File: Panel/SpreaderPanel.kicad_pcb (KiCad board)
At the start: 2 copper layers, 50 x 200 mm, 7 parts

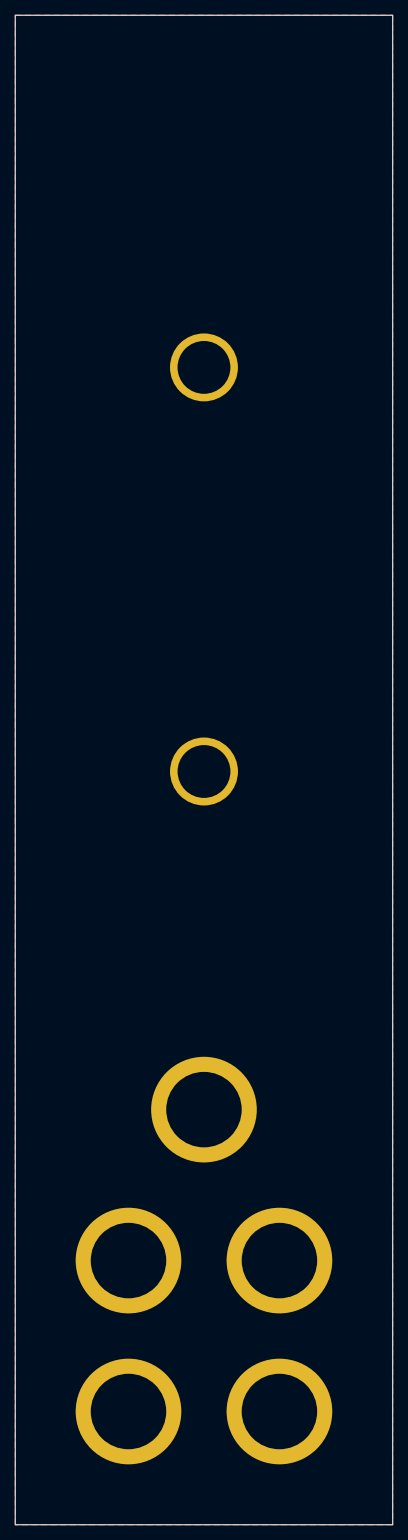
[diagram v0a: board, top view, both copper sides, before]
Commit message: Add panel text
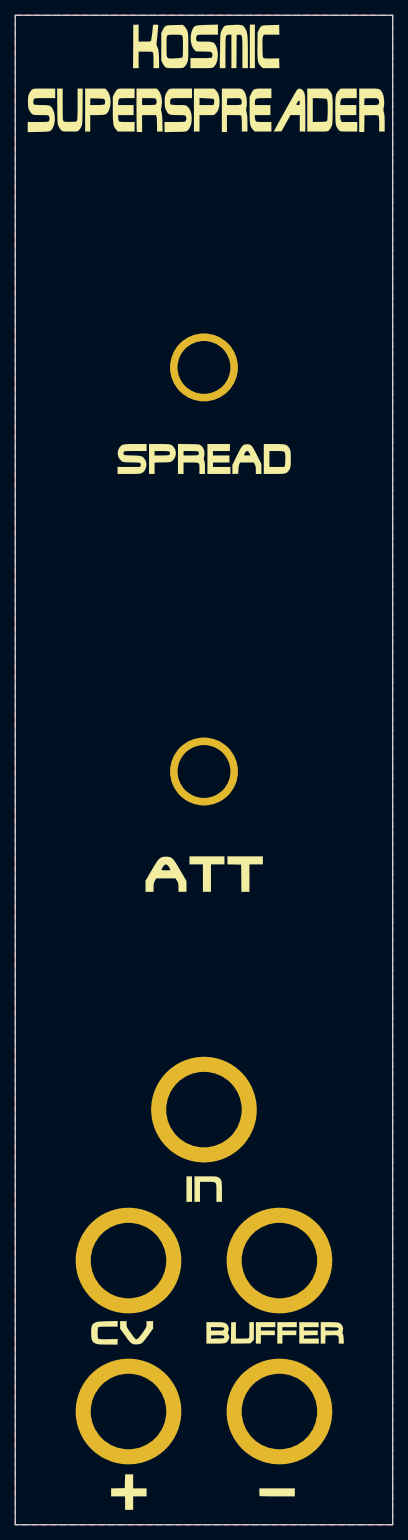
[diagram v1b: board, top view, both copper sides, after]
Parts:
- added G***: LOGO, Sonosus:SuperSilk, F.Cu at (126.9, 125.8)
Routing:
- added copper zone on B.Cu, net GND

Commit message: Add JLC order no and licensing info
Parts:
- added REF**: Kosmo_Panel_Slotted_Mounting_Hole, Sonosus:Kosmo_Panel_Slotted_Mounting_Hole, F.Cu at (104.9, 222.8)
- added REF**: Kosmo_Panel_Slotted_Mounting_Hole, Sonosus:Kosmo_Panel_Slotted_Mounting_Hole, F.Cu at (145.9, 222.8)
- added REF**: Kosmo_Panel_Slotted_Mounting_Hole, Sonosus:Kosmo_Panel_Slotted_Mounting_Hole, F.Cu at (145.9, 28.8)
- added REF**: Kosmo_Panel_Slotted_Mounting_Hole, Sonosus:Kosmo_Panel_Slotted_Mounting_Hole, F.Cu at (104.9, 28.8)
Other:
- board text added: "JLCJLCJLCJLC"
- board text added: "SS-06 Kosmic Superspreader CC-BY-SA Panel by Sonosus June 2021"
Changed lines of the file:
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@@
   (general
     (thickness 1.6)
-    (drawings 4)
+    (drawings 6)
     (tracks 0)
     (zones 0)
-    (modules 8)
+    (modules 12)
     (nets 2)
   )
@@
     (mod_text_size 1 1)
     (mod_text_width 0.15)
-    (pad_size 14 14)
-    (pad_drill 10)
+    (pad_size 6.8 4)
+    (pad_drill 6)
     (pad_to_mask_clearance 0)
     (aux_axis_origin 0 0)
@@
     (uvia_drill 0.1)
     (add_net GND)
+  )
+  (module Sonosus:Kosmo_Panel_Slotted_Mounting_Hole (layer F.Cu)
+    (at 104.873 222.81)
+    (descr "Mounting Hole 3.2mm, M3")
+    (tags "mounting hole 3.2mm m3")
+    (attr virtual)
+    (fp_text reference REF** (at 1.4 -4.2) (layer F.SilkS) hide
+      (effects (font (size 1 1) (thickness 0.15)))
+    )
+    (fp_text value Kosmo_Panel_Slotted_Mounting_Hole (at 1.4 4.2) (layer F.Fab)
+      (effects (font (size 1 1) (thickness 0.15)))
+    )
+    (fp_line (start 0 3.25) (end 2.8 3.25) (layer F.CrtYd) (width 0.05))
+    (fp_line (start 0 -3.25) (end 2.8 -3.25) (layer F.CrtYd) (width 0.05))
+    (fp_line (start 0 3) (end 2.8 3) (layer Cmts.User) (width 0.12))
+    (fp_line (start 0 -3) (end 2.8 -3) (layer Cmts.User) (width 0.12))
+    (fp_text user %R (at 1.7 0) (layer F.Fab)
+      (effects (font (size 1 1) (thickness 0.15)))
+    )
+    (fp_arc (start 2.8 0) (end 2.8 3) (angle -180) (layer Cmts.User) (width 0.12))
+    (fp_arc (start 0 0) (end 0 -3) (angle -180) (layer Cmts.User) (width 0.12))
+    (fp_arc (start 2.8 0) (end 2.8 3.25) (angle -180) (layer F.CrtYd) (width 0.05))
+    (fp_arc (start 0 0) (end 0 3.25) (angle 180) (layer F.CrtYd) (width 0.05))
+    (pad 1 thru_hole oval (at 1.4 0) (size 6.8 4) (drill oval 6 3.2) (layers *.Cu *.Mask)
+      (net 1 GND))
+  )
+  (module Sonosus:Kosmo_Panel_Slotted_Mounting_Hole (layer F.Cu)
+    (at 145.873 222.81)
+    (descr "Mounting Hole 3.2mm, M3")
+    (tags "mounting hole 3.2mm m3")
+    (attr virtual)
+    (fp_text reference REF** (at 1.4 -4.2) (layer F.SilkS) hide
+      (effects (font (size 1 1) (thickness 0.15)))
+    )
+    (fp_text value Kosmo_Panel_Slotted_Mounting_Hole (at 1.4 4.2) (layer F.Fab)
+      (effects (font (size 1 1) (thickness 0.15)))
+    )
+    (fp_line (start 0 3.25) (end 2.8 3.25) (layer F.CrtYd) (width 0.05))
+    (fp_line (start 0 -3.25) (end 2.8 -3.25) (layer F.CrtYd) (width 0.05))
+    (fp_line (start 0 3) (end 2.8 3) (layer Cmts.User) (width 0.12))
+    (fp_line (start 0 -3) (end 2.8 -3) (layer Cmts.User) (width 0.12))
+    (fp_text user %R (at 1.7 0) (layer F.Fab)
+      (effects (font (size 1 1) (thickness 0.15)))
+    )
+    (fp_arc (start 2.8 0) (end 2.8 3) (angle -180) (layer Cmts.User) (width 0.12))
+    (fp_arc (start 0 0) (end 0 -3) (angle -180) (layer Cmts.User) (width 0.12))
+    (fp_arc (start 2.8 0) (end 2.8 3.25) (angle -180) (layer F.CrtYd) (width 0.05))
+    (fp_arc (start 0 0) (end 0 3.25) (angle 180) (layer F.CrtYd) (width 0.05))
+    (pad 1 thru_hole oval (at 1.4 0) (size 6.8 4) (drill oval 6 3.2) (layers *.Cu *.Mask)
+      (net 1 GND))
+  )
+  (module Sonosus:Kosmo_Panel_Slotted_Mounting_Hole (layer F.Cu)
+    (at 145.873 28.81)
+    (descr "Mounting Hole 3.2mm, M3")
+    (tags "mounting hole 3.2mm m3")
+    (attr virtual)
+    (fp_text reference REF** (at 1.4 -4.2) (layer F.SilkS) hide
+      (effects (font (size 1 1) (thickness 0.15)))
+    )
+    (fp_text value Kosmo_Panel_Slotted_Mounting_Hole (at 1.4 4.2) (layer F.Fab)
+      (effects (font (size 1 1) (thickness 0.15)))
+    )
+    (fp_line (start 0 3.25) (end 2.8 3.25) (layer F.CrtYd) (width 0.05))
+    (fp_line (start 0 -3.25) (end 2.8 -3.25) (layer F.CrtYd) (width 0.05))
+    (fp_line (start 0 3) (end 2.8 3) (layer Cmts.User) (width 0.12))
+    (fp_line (start 0 -3) (end 2.8 -3) (layer Cmts.User) (width 0.12))
+    (fp_text user %R (at 1.7 0) (layer F.Fab)
+      (effects (font (size 1 1) (thickness 0.15)))
+    )
+    (fp_arc (start 2.8 0) (end 2.8 3) (angle -180) (layer Cmts.User) (width 0.12))
+    (fp_arc (start 0 0) (end 0 -3) (angle -180) (layer Cmts.User) (width 0.12))
+    (fp_arc (start 2.8 0) (end 2.8 3.25) (angle -180) (layer F.CrtYd) (width 0.05))
+    (fp_arc (start 0 0) (end 0 3.25) (angle 180) (layer F.CrtYd) (width 0.05))
+    (pad 1 thru_hole oval (at 1.4 0) (size 6.8 4) (drill oval 6 3.2) (layers *.Cu *.Mask)
+      (net 1 GND))
+  )
+  (module Sonosus:Kosmo_Panel_Slotted_Mounting_Hole (layer F.Cu)
+    (at 104.873 28.81)
+    (descr "Mounting Hole 3.2mm, M3")
+    (tags "mounting hole 3.2mm m3")
+    (attr virtual)
+    (fp_text reference REF** (at 1.4 -4.2) (layer F.SilkS) hide
+      (effects (font (size 1 1) (thickness 0.15)))
+    )
+    (fp_text value Kosmo_Panel_Slotted_Mounting_Hole (at 1.4 4.2) (layer F.Fab)
+      (effects (font (size 1 1) (thickness 0.15)))
+    )
+    (fp_arc (start 0 0) (end 0 3.25) (angle 180) (layer F.CrtYd) (width 0.05))
+    (fp_arc (start 2.8 0) (end 2.8 3.25) (angle -180) (layer F.CrtYd) (width 0.05))
+    (fp_arc (start 0 0) (end 0 -3) (angle -180) (layer Cmts.User) (width 0.12))
+    (fp_arc (start 2.8 0) (end 2.8 3) (angle -180) (layer Cmts.User) (width 0.12))
+    (fp_text user %R (at 1.7 0) (layer F.Fab)
+      (effects (font (size 1 1) (thickness 0.15)))
+    )
+    (fp_line (start 0 3.25) (end 2.8 3.25) (layer F.CrtYd) (width 0.05))
+    (fp_line (start 0 -3.25) (end 2.8 -3.25) (layer F.CrtYd) (width 0.05))
+    (fp_line (start 0 3) (end 2.8 3) (layer Cmts.User) (width 0.12))
+    (fp_line (start 0 -3) (end 2.8 -3) (layer Cmts.User) (width 0.12))
+    (pad 1 thru_hole oval (at 1.4 0) (size 6.8 4) (drill oval 6 3.2) (layers *.Cu *.Mask)
+      (net 1 GND))
   )
   (module Sonosus:SuperSilk (layer F.Cu)
@@
       (net 1 GND))
   )
+  (gr_text "SS-06 Kosmic Superspreader\nCC-BY-SA\nPanel by Sonosus June 2021" (at 126.873 49.81) (layer B.SilkS)
+    (effects (font (size 2 2) (thickness 0.35)) (justify mirror))
+  )
+  (gr_text JLCJLCJLCJLC (at 121.873 96.81) (layer B.SilkS)
+    (effects (font (size 3 3) (thickness 0.3)) (justify mirror))
+  )
   (gr_line (start 151.873 25.81) (end 151.873 225.81) (layer Edge.Cuts) (width 0.05))
